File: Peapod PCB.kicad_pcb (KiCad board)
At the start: 2 copper layers, 70.9 x 26.9 mm, 20 parts, among them U1 ESP8266

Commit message: Total re work
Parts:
- moved GPIO5 24.3 mm to (174.8, 29.5)
- moved TX 17.0 mm to (220.5, 33.3)
- moved GPIO4 13.5 mm to (208.0, 50.3)
- moved GPIO0 13.2 mm to (217.4, 50.3), turned to 180 degrees
- moved BRDG 2 RESET 10.4 mm to (165.4, 29.5)
- moved ANALOG 10.2 mm to (156.0, 29.5)
- moved R1 9.17 mm to (169.9, 38.1)
- moved R2 9.16 mm to (169.9, 34.8)
- moved RX 8.46 mm to (220.5, 43.9)
- moved FTDI 3.3V 6.29 mm to (221.5, 28.4)
- moved U1 5.86 mm to (184.9, 35.1)
- moved VOTE :| 4.06 mm to (166.1, 47.0)
- moved VOTE :( 3.56 mm to (175.5, 47.0)
- moved VOTE :) 3.05 mm to (157.0, 47.0)
- moved R4 1.63 mm to (206.8, 36.8)
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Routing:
- net +3V3: track 118.3 -> 78.0 mm
- net Net-(BTN2-Pad2): track 31.0 -> 0.00 mm
- net GND: track 23.6 -> 0.00 mm, vias 6 -> 0
- net Net-(J2-Pad1): track 14.6 -> 30.8 mm
- net Net-(J3-Pad5): track 45.1 -> 30.1 mm, vias 2 -> 4
- net Net-(J3-Pad4): track 32.7 -> 19.4 mm, vias 2 -> 1
- net Net-(J7-Pad1): track 27.2 -> 40.1 mm
- net Net-(R1-Pad1): track 9.45 -> 17.4 mm
- net Net-(J6-Pad1): track 18.8 -> 24.4 mm
- net Net-(R3-Pad2): track 5.56 -> 11.0 mm
- net Net-(R5-Pad1): track 5.83 -> 10.1 mm
- net Net-(BTN1-Pad2): track 20.0 -> 22.4 mm
- net Net-(J5-Pad1): track 25.9 -> 28.1 mm, vias 0 -> 2
- net Net-(BTN3-Pad2): track 11.5 -> 12.4 mm

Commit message: updated runs
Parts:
- moved TX 46.1 mm to (174.5, 29.5)
- moved GPIO5 39.0 mm to (207.8, 50.3)
- moved RX 9.40 mm to (220.5, 34.5)
- moved GPIO4 5.84 mm to (213.9, 50.3)
- moved GPIO0 4.31 mm to (220.5, 47.2), turned to 90 degrees
- moved VOTE :) 3.06 mm to (160.0, 47.2)
- moved VOTE :| 2.55 mm to (168.7, 47.2)
- moved R5 2.34 mm to (208.5, 40.9), turned to 90 degrees
- moved VOTE :( 2.30 mm to (177.8, 47.2)
- moved R4 2.29 mm to (204.5, 36.8)
- moved R3 1.48 mm to (206.0, 40.9), turned to 270 degrees
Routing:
- net +3V3: track 78.0 -> 111.9 mm, vias 0 -> 2
- net Net-(BTN2-Pad2): track 0.00 -> 28.7 mm
- net Net-(J3-Pad4): track 19.4 -> 32.9 mm, vias 1 -> 3
- net Net-(J6-Pad1): track 24.4 -> 36.4 mm
- net Net-(J3-Pad5): track 30.1 -> 41.9 mm, vias 4 -> 0
- net Net-(J7-Pad1): track 40.1 -> 45.6 mm
- net Net-(BTN1-Pad2): track 22.4 -> 19.8 mm
- net Net-(J5-Pad1): track 28.1 -> 30.7 mm, vias 2 -> 0
- net Net-(R3-Pad2): track 11.0 -> 9.09 mm
- net Net-(R5-Pad1): track 10.1 -> 11.9 mm
- net Net-(J2-Pad1): track 30.8 -> 29.1 mm
- net Net-(BTN3-Pad2): track 12.4 -> 11.1 mm

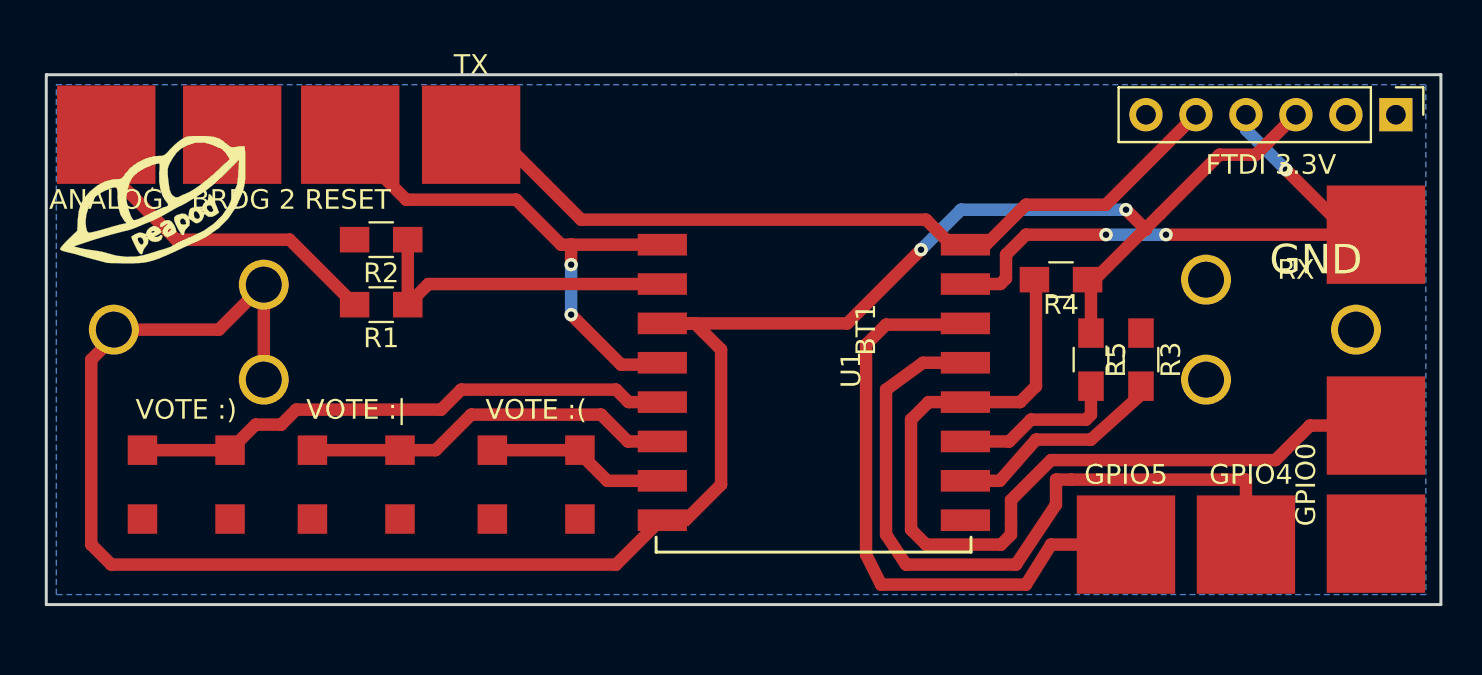
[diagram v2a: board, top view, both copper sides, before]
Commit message: Added keep out
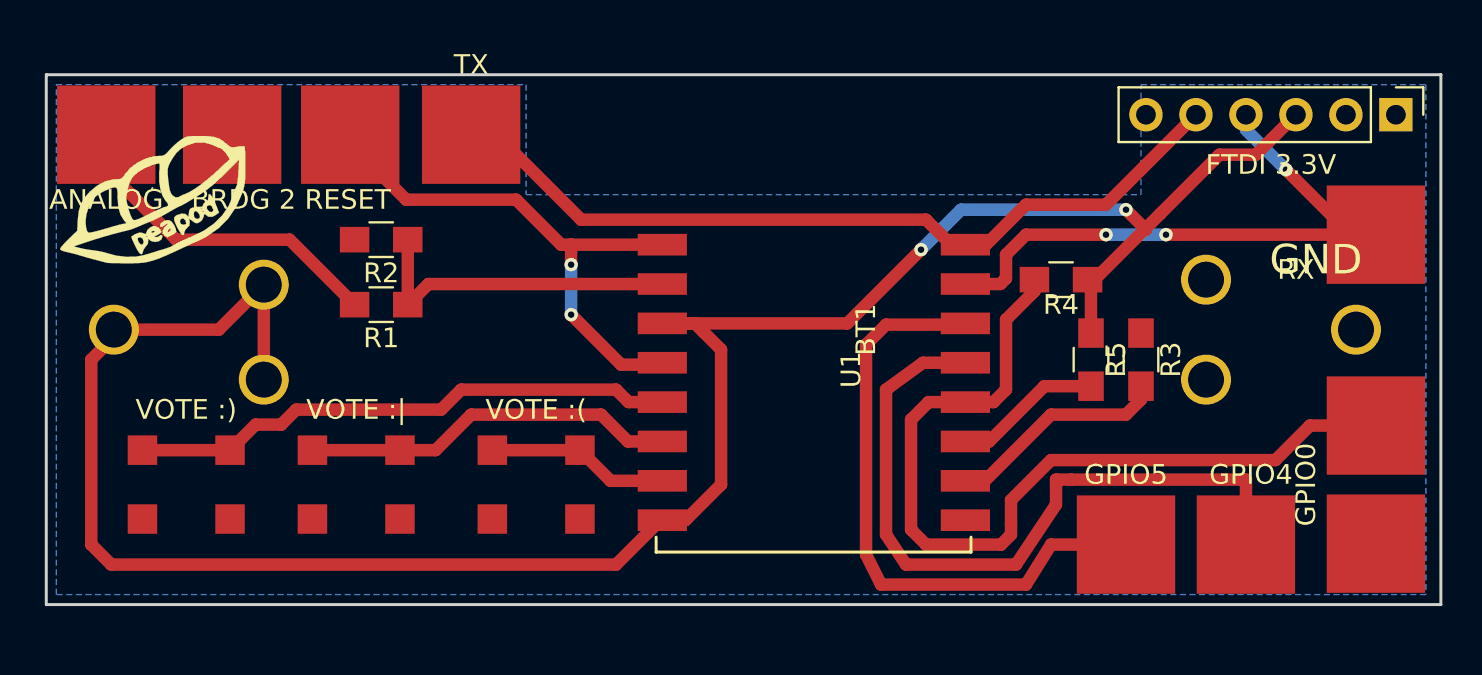
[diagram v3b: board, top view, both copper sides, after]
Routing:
- net Net-(BTN3-Pad2): track 11.1 -> 9.98 mm
- net Net-(J7-Pad1): track 45.6 -> 44.7 mm
- net Net-(R3-Pad2): track 9.09 -> 8.25 mm
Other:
- outline, holes or cut-outs redrawn
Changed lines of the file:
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@@
     (area 152.832999 26.340999 223.849001 53.415001)
     (thickness 1.6002)
-    (drawings 7)
-    (tracks 139)
+    (drawings 6)
+    (tracks 136)
     (zones 0)
     (modules 20)
@@
     (trace_clearance 0.1524)
     (zone_clearance 0.508)
-    (zone_45_only no)
+    (zone_45_only yes)
     (trace_min 0.1524)
     (segment_width 0.2)
@@
       (xy -1.27 2.44475)) (layer B.SilkS) (width 0.01))
   )
+  (gr_line (start 152.908 26.416) (end 223.774 26.416) (angle 90) (layer Edge.Cuts) (width 0.15))
   (gr_text GND (at 217.424 35.814) (layer F.SilkS)
     (effects (font (size 1.5 1.5) (thickness 0.3)))
   )
-  (gr_line (start 152.908 26.416) (end 202.184 26.416) (angle 90) (layer Edge.Cuts) (width 0.15))
   (gr_line (start 152.908 53.34) (end 152.908 26.416) (angle 90) (layer Edge.Cuts) (width 0.15))
   (gr_line (start 223.774 53.34) (end 152.908 53.34) (angle 90) (layer Edge.Cuts) (width 0.15))
   (gr_line (start 223.774 26.416) (end 223.774 53.34) (angle 90) (layer Edge.Cuts) (width 0.15))
-  (gr_line (start 202.184 26.416) (end 223.774 26.416) (angle 90) (layer Edge.Cuts) (width 0.15))
   (gr_text "FSOSS 2017" (at 188.468 32.512) (layer B.SilkS)
     (effects (font (size 6 7) (thickness 0.3)) (justify mirror))
@@
   (segment (start 181.864 42.418) (end 182.498 43.052) (width 0.635) (layer F.Cu) (net 4))
   (segment (start 182.498 43.052) (end 184.912 43.052) (width 0.635) (layer F.Cu) (net 4))
-  (segment (start 175.575 45.494) (end 180.025 45.494) (width 0.635) (layer F.Cu) (net 5) (status 30))
-  (segment (start 180.025 45.494) (end 180.053 45.466) (width 0.635) (layer F.Cu) (net 5) (status 30))
-  (segment (start 180.053 45.466) (end 179.578 45.212) (width 0.635) (layer F.Cu) (net 5) (status 10))
-  (segment (start 179.578 45.212) (end 181.418 47.052) (width 0.635) (layer F.Cu) (net 5))
-  (segment (start 181.418 47.052) (end 184.912 47.052) (width 0.635) (layer F.Cu) (net 5))
+  (segment (start 175.575 45.494) (end 180.025 45.494) (width 0.635) (layer F.Cu) (net 5) (status C00000))
+  (segment (start 180.025 45.494) (end 181.583 47.052) (width 0.635) (layer F.Cu) (net 5) (status 400000))
+  (segment (start 181.583 47.052) (end 184.912 47.052) (width 0.635) (layer F.Cu) (net 5) (status 800000))
   (segment (start 155.956 29.464) (end 155.956 31.242) (width 0.635) (layer F.Cu) (net 6))
   (segment (start 155.956 31.242) (end 159.512 34.798) (width 0.635) (layer F.Cu) (net 6))
@@
   (segment (start 213.614 46.99) (end 204.978 46.99) (width 0.635) (layer F.Cu) (net 13))
   (segment (start 213.868 46.99) (end 213.614 46.99) (width 0.635) (layer F.Cu) (net 13))
+  (segment (start 203.12 36.83) (end 203.12 37.418) (width 0.635) (layer F.Cu) (net 14))
+  (segment (start 203.12 37.418) (end 201.676 38.862) (width 0.635) (layer F.Cu) (net 14))
+  (segment (start 201.676 38.862) (end 201.676 42.418) (width 0.635) (layer F.Cu) (net 14))
+  (segment (start 201.676 42.418) (end 201.042 43.052) (width 0.635) (layer F.Cu) (net 14))
+  (segment (start 201.042 43.052) (end 198.912 43.052) (width 0.635) (layer F.Cu) (net 14))
   (segment (start 220.472 44.244) (end 217.122 44.244) (width 0.635) (layer F.Cu) (net 14))
   (segment (start 197.74 43.052) (end 198.912 43.052) (width 0.635) (layer F.Cu) (net 14))
@@
   (segment (start 215.366598 45.999402) (end 203.962 45.999402) (width 0.635) (layer F.Cu) (net 14))
   (segment (start 217.122 44.244) (end 215.366598 45.999402) (width 0.635) (layer F.Cu) (net 14))
-  (segment (start 203.2 36.91) (end 203.2 42.244) (width 0.635) (layer F.Cu) (net 14))
-  (segment (start 202.392 43.052) (end 203.2 42.244) (width 0.635) (layer F.Cu) (net 14))
-  (segment (start 202.392 43.052) (end 198.912 43.052) (width 0.635) (layer F.Cu) (net 14))
-  (segment (start 203.2 36.91) (end 203.12 36.83) (width 0.635) (layer F.Cu) (net 14))
   (segment (start 171.276 34.798) (end 171.276 38.1) (width 0.635) (layer F.Cu) (net 15))
   (segment (start 171.276 38.1) (end 172.324 37.052) (width 0.635) (layer F.Cu) (net 15))
   (segment (start 172.324 37.052) (end 184.912 37.052) (width 0.635) (layer F.Cu) (net 15))
-  (segment (start 198.912 45.052) (end 201.836 45.052) (width 0.635) (layer F.Cu) (net 16))
-  (segment (start 205.994 43.688) (end 205.994 42.244) (width 0.635) (layer F.Cu) (net 16))
-  (segment (start 205.74 43.942) (end 205.994 43.688) (width 0.635) (layer F.Cu) (net 16))
-  (segment (start 202.946 43.942) (end 205.74 43.942) (width 0.635) (layer F.Cu) (net 16))
-  (segment (start 201.836 45.052) (end 202.946 43.942) (width 0.635) (layer F.Cu) (net 16))
-  (segment (start 198.912 47.052) (end 201.36 47.052) (width 0.635) (layer F.Cu) (net 17))
-  (segment (start 205.994 44.958) (end 208.534 42.672) (width 0.635) (layer F.Cu) (net 17))
-  (segment (start 203.2 44.958) (end 205.994 44.958) (width 0.635) (layer F.Cu) (net 17))
-  (segment (start 201.36 47.052) (end 203.2 44.958) (width 0.635) (layer F.Cu) (net 17))
-  (segment (start 208.534 42.672) (end 208.534 42.244) (width 0.635) (layer F.Cu) (net 17))
-  (zone (net 2) (net_name GND) (layer B.Cu) (hatch edge 0.508)
+  (segment (start 205.994 42.244) (end 203.628 42.244) (width 0.635) (layer F.Cu) (net 16))
+  (segment (start 203.628 42.244) (end 200.82 45.052) (width 0.635) (layer F.Cu) (net 16))
+  (segment (start 200.82 45.052) (end 198.912 45.052) (width 0.635) (layer F.Cu) (net 16))
+  (segment (start 208.534 42.244) (end 208.534 42.926) (width 0.635) (layer F.Cu) (net 17))
+  (segment (start 208.534 42.926) (end 207.772 43.688) (width 0.635) (layer F.Cu) (net 17))
+  (segment (start 207.772 43.688) (end 203.962 43.688) (width 0.635) (layer F.Cu) (net 17))
+  (segment (start 203.962 43.688) (end 200.598 47.052) (width 0.635) (layer F.Cu) (net 17))
+  (segment (start 200.598 47.052) (end 198.912 47.052) (width 0.635) (layer F.Cu) (net 17))
+  (zone (net 2) (net_name GND) (layer B.Cu) (hatch none 0.508)
     (connect_pads (clearance 0.508))
     (min_thickness 0.254)
@@
     (polygon
       (pts
-        (xy 223.012 52.832) (xy 153.416 52.832) (xy 153.416 26.924) (xy 223.012 26.924)
+        (xy 177.292 32.512) (xy 208.534 32.512) (xy 208.534 26.924) (xy 223.012 26.924) (xy 223.012 52.832)
+        (xy 153.416 52.832) (xy 153.416 26.924) (xy 177.292 26.924)
       )
     )

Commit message: Moved zone outline
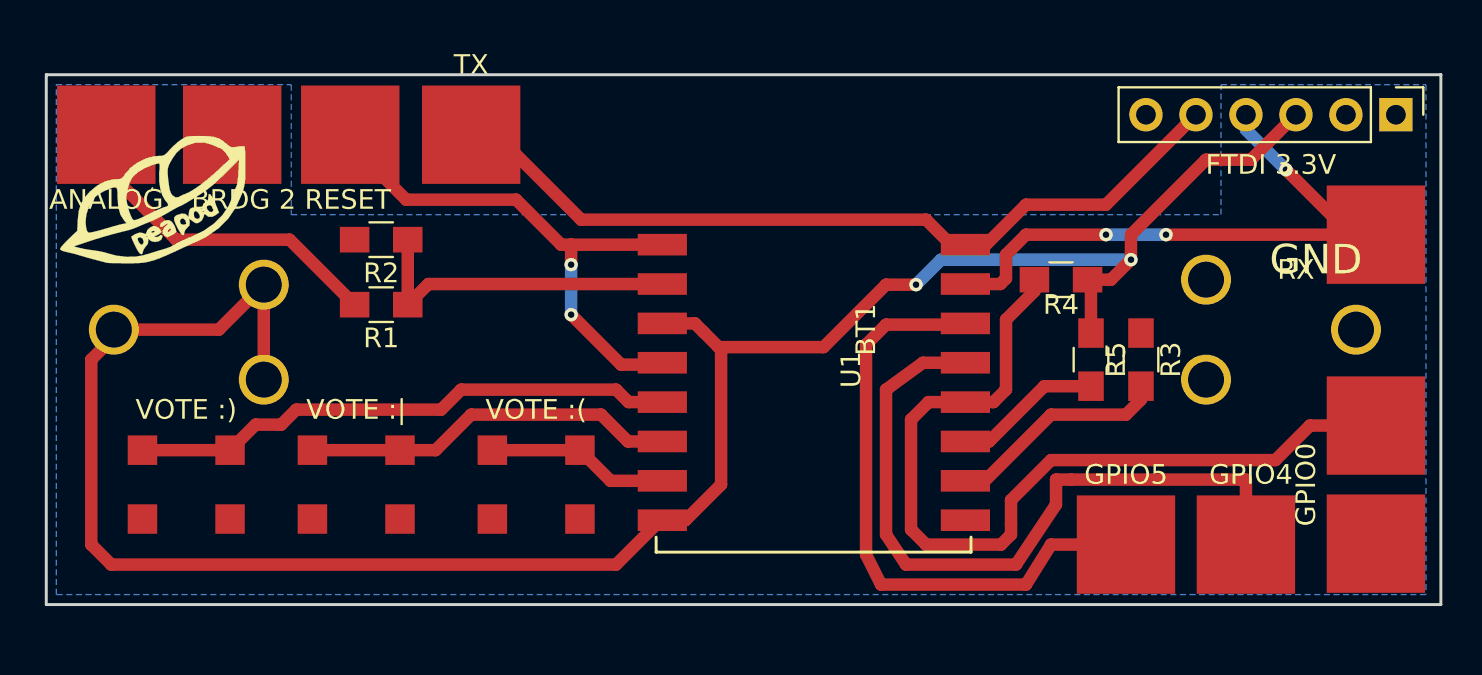
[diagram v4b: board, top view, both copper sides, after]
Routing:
- net +3V3: track 111.9 -> 108.7 mm
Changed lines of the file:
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@@
     (effects (font (size 6 7) (thickness 0.3)) (justify mirror))
   )
-  (segment (start 184.912 39.052) (end 193.612 39.052) (width 0.635) (layer F.Cu) (net 1))
-  (segment (start 208.788 34.29) (end 208.788 34.21) (width 0.635) (layer F.Cu) (net 1))
-  (segment (start 208.748 34.25) (end 208.788 34.29) (width 0.635) (layer F.Cu) (net 1))
-  (segment (start 207.772 33.274) (end 208.748 34.25) (width 0.635) (layer F.Cu) (net 1))
-  (via (at 207.772 33.274) (size 0.6858) (drill 0.3302) (layers F.Cu B.Cu) (net 1))
-  (segment (start 199.39 33.274) (end 207.772 33.274) (width 0.635) (layer B.Cu) (net 1))
-  (segment (start 197.358 35.306) (end 199.39 33.274) (width 0.635) (layer B.Cu) (net 1))
-  (via (at 197.358 35.306) (size 0.6858) (drill 0.3302) (layers F.Cu B.Cu) (net 1))
-  (segment (start 193.612 39.052) (end 197.358 35.306) (width 0.635) (layer F.Cu) (net 1))
+  (segment (start 208.026 35.814) (end 208.026 34.544) (width 0.635) (layer F.Cu) (net 1))
+  (segment (start 214.122 30.734) (end 216.408 28.448) (width 0.635) (layer F.Cu) (net 1) (status 800000))
+  (segment (start 211.836 30.734) (end 214.122 30.734) (width 0.635) (layer F.Cu) (net 1))
+  (segment (start 208.026 34.544) (end 211.836 30.734) (width 0.635) (layer F.Cu) (net 1))
+  (segment (start 187.071 40.259) (end 192.405 40.259) (width 0.635) (layer F.Cu) (net 1))
+  (segment (start 207.01 36.83) (end 205.82 36.83) (width 0.635) (layer F.Cu) (net 1) (status 800000))
+  (segment (start 208.026 35.814) (end 207.01 36.83) (width 0.635) (layer F.Cu) (net 1))
+  (via (at 208.026 35.814) (size 0.6858) (drill 0.3302) (layers F.Cu B.Cu) (net 1))
+  (segment (start 198.374 35.814) (end 208.026 35.814) (width 0.635) (layer B.Cu) (net 1))
+  (segment (start 197.104 37.084) (end 198.374 35.814) (width 0.635) (layer B.Cu) (net 1))
+  (via (at 197.104 37.084) (size 0.6858) (drill 0.3302) (layers F.Cu B.Cu) (net 1))
+  (segment (start 195.58 37.084) (end 197.104 37.084) (width 0.635) (layer F.Cu) (net 1))
+  (segment (start 192.405 40.259) (end 195.58 37.084) (width 0.635) (layer F.Cu) (net 1))
   (segment (start 184.912 49.052) (end 185.39 49.052) (width 0.635) (layer F.Cu) (net 1))
   (segment (start 185.39 49.052) (end 187.198 47.244) (width 0.635) (layer F.Cu) (net 1))
   (segment (start 185.864 39.052) (end 184.912 39.052) (width 0.635) (layer F.Cu) (net 1))
-  (segment (start 187.198 40.386) (end 186.309 39.497) (width 0.635) (layer F.Cu) (net 1))
+  (segment (start 187.198 40.386) (end 187.071 40.259) (width 0.635) (layer F.Cu) (net 1))
+  (segment (start 187.071 40.259) (end 186.309 39.497) (width 0.635) (layer F.Cu) (net 1))
   (segment (start 186.309 39.497) (end 185.864 39.052) (width 0.635) (layer F.Cu) (net 1))
   (segment (start 187.198 47.244) (end 187.198 40.386) (width 0.635) (layer F.Cu) (net 1))
   (segment (start 205.994 39.544) (end 205.994 37.004) (width 0.635) (layer F.Cu) (net 1))
-  (segment (start 205.994 37.004) (end 208.788 34.21) (width 0.635) (layer F.Cu) (net 1))
-  (segment (start 208.788 34.21) (end 209.51 33.488) (width 0.635) (layer F.Cu) (net 1))
-  (segment (start 212.518 30.48) (end 214.376 30.48) (width 0.635) (layer F.Cu) (net 1))
-  (segment (start 214.376 30.48) (end 216.408 28.448) (width 0.635) (layer F.Cu) (net 1))
-  (segment (start 209.51 33.488) (end 212.518 30.48) (width 0.635) (layer F.Cu) (net 1))
   (segment (start 156.34 39.37) (end 156.34 39.748) (width 0.635) (layer F.Cu) (net 1))
   (segment (start 156.34 39.748) (end 155.194 40.894) (width 0.635) (layer F.Cu) (net 1))
@@
     (polygon
       (pts
-        (xy 177.292 32.512) (xy 208.534 32.512) (xy 208.534 26.924) (xy 223.012 26.924) (xy 223.012 52.832)
-        (xy 153.416 52.832) (xy 153.416 26.924) (xy 177.292 26.924)
+        (xy 165.354 33.528) (xy 212.598 33.528) (xy 212.598 26.924) (xy 223.012 26.924) (xy 223.012 52.832)
+        (xy 153.416 52.832) (xy 153.416 26.924) (xy 165.354 26.924)
       )
     )

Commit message: Tuned the routing
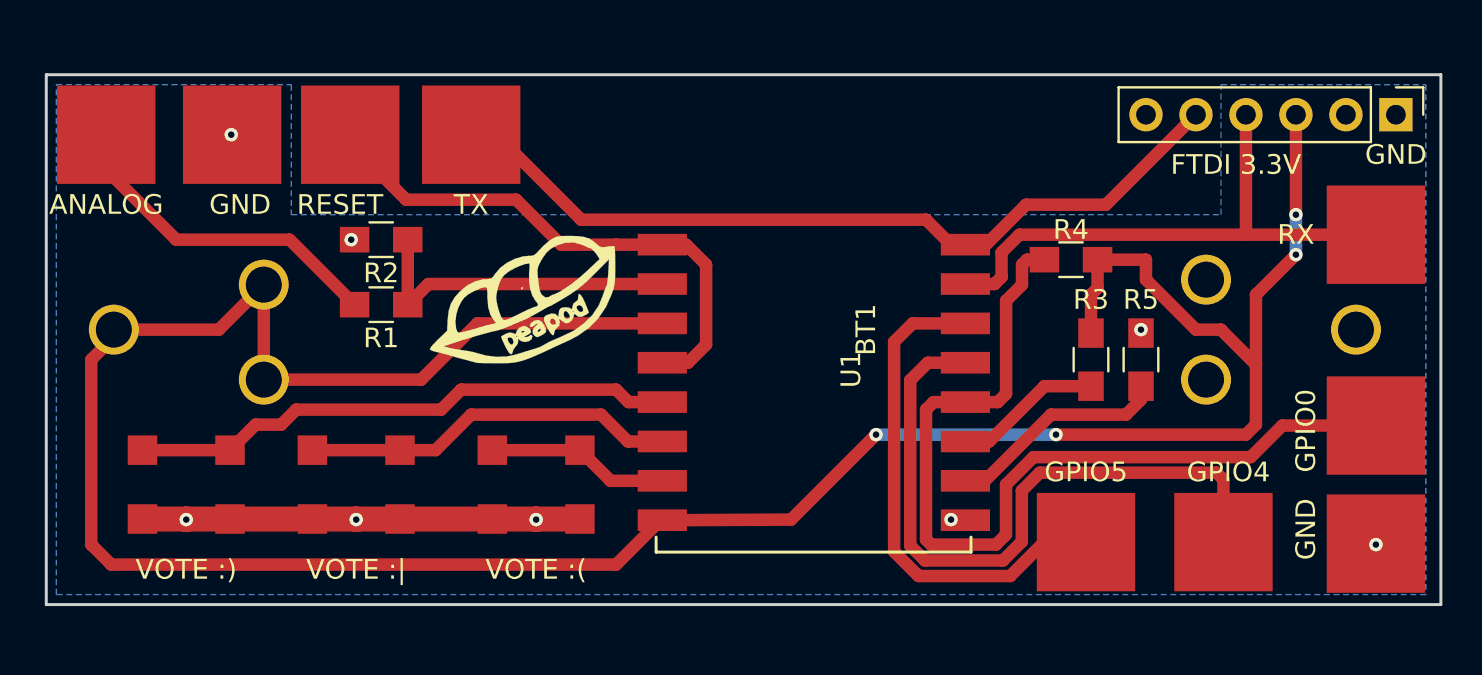
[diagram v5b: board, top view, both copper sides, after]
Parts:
- GND   GPIO0: renamed from GPIO0
- GND   RESET: renamed from BRDG 2 RESET
- moved G*** 19.5 mm to (177.3, 38.1)
- moved GPIO5 2.04 mm to (205.7, 50.2)
- moved GPIO4 1.15 mm to (212.7, 50.2)
- moved R4 1.14 mm to (205.0, 35.8)
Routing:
- net +3V3: track 108.7 -> 140.8 mm, vias 2 -> 4
- net GND: track 0.00 -> 22.3 mm, vias 0 -> 8
- net Net-(J5-Pad1): track 30.7 -> 25.0 mm
- net Net-(J6-Pad1): track 36.4 -> 33.8 mm
- net Net-(J3-Pad4): track 32.9 -> 30.7 mm, vias 3 -> 0
- net Net-(J2-Pad1): track 29.1 -> 27.1 mm, vias 2 -> 0
- net Net-(J7-Pad1): track 44.7 -> 46.1 mm
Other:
- board text added: "+"
- board text added: "-"
- board text added: "ANALOG 3.3v to 1v R2 = 10k R1 = 25k"
